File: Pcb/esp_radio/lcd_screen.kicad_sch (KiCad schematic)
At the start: 7 parts, among them J7 LCD I2C, J8 LCD SPI, Q1 AO3415A

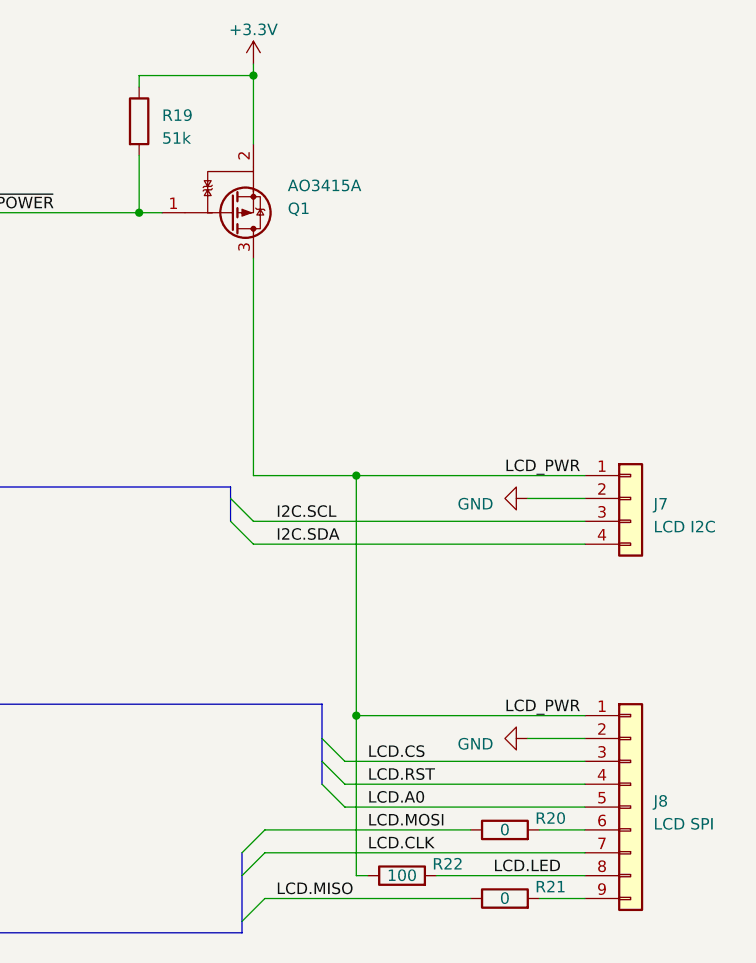
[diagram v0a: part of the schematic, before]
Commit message: Move custom components to kicad_common_library.
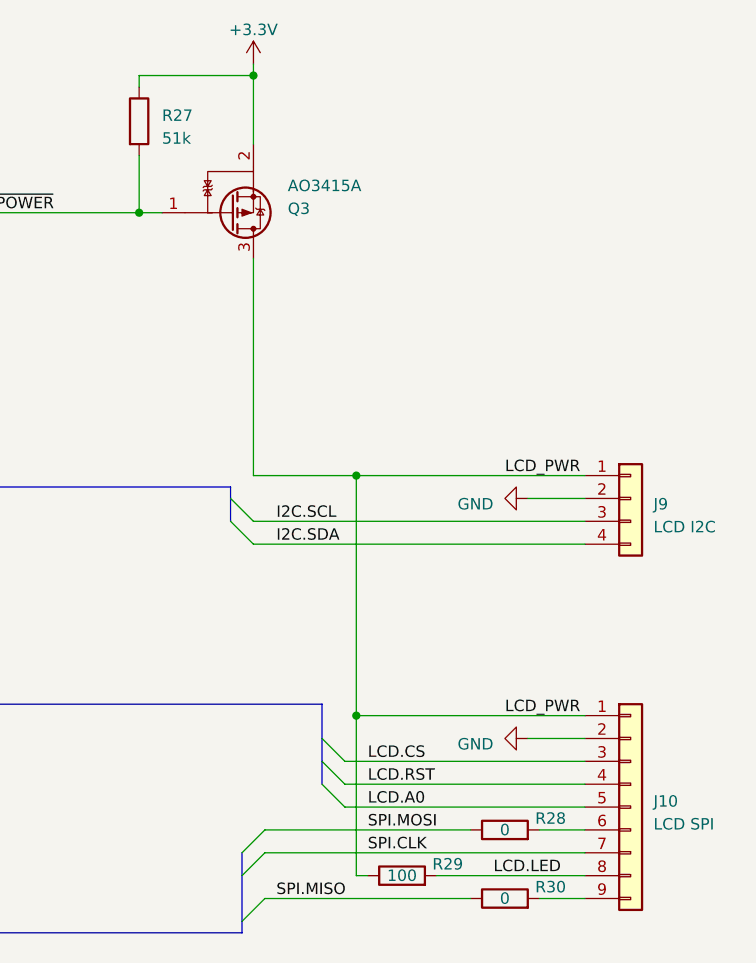
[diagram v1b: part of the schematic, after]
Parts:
- Q3: renamed from Q1; symbol AO3415A:AO3401A -> kicad_common_lib:AO3415A
- renumbered J8 to J10, J7 to J9, R19 to R27, R20 to R28, R22 to R29, R21 to R30
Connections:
- net LCD.CLK renamed SPI.CLK
- net LCD.MISO renamed SPI.MISO
- net LCD.MOSI renamed SPI.MOSI
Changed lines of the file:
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@@
     (effects (font (size 1.27 1.27)) (justify left bottom))
   )
-  (label "LCD.MOSI" (at 185.42 127 0) (fields_autoplaced)
+  (label "SPI.MOSI" (at 185.42 127 0) (fields_autoplaced)
     (effects (font (size 1.27 1.27)) (justify left bottom))
   )
@@
     (effects (font (size 1.27 1.27)) (justify left bottom))
   )
-  (label "LCD.MISO" (at 175.26 134.62 0) (fields_autoplaced)
+  (label "SPI.MISO" (at 175.26 134.62 0) (fields_autoplaced)
     (effects (font (size 1.27 1.27)) (justify left bottom))
   )
@@
     (effects (font (size 1.27 1.27)) (justify left bottom))
   )
-  (label "LCD.CLK" (at 185.42 129.54 0) (fields_autoplaced)
+  (label "SPI.CLK" (at 185.42 129.54 0) (fields_autoplaced)
     (effects (font (size 1.27 1.27)) (justify left bottom))
   )
@@
   (symbol (lib_id "Device:R") (at 200.66 134.62 90) (unit 1)
     (in_bom yes) (on_board yes) (dnp no)
-    (property "Reference" "R21" (at 205.74 133.35 90)
+    (property "Reference" "R30" (at 205.74 133.35 90)
       (effects (font (size 1.27 1.27)))
     )
@@
       (project "esp_radio"
         (path "/c9e2e0d2-0655-4f5e-8e13-71b41b1f7cfe/9a87a4f6-9f89-4802-b675-78042b654f8a"
-          (reference "R21") (unit 1)
+          (reference "R30") (unit 1)
         )
       )
@@
   (symbol (lib_id "Connector_Generic:Conn_01x09") (at 214.63 124.46 0) (unit 1)
     (in_bom yes) (on_board yes) (dnp no) (fields_autoplaced)
-    (property "Reference" "J8" (at 217.17 123.825 0)
+    (property "Reference" "J10" (at 217.17 123.825 0)
       (effects (font (size 1.27 1.27)) (justify left))
     )
@@
       (project "esp_radio"
         (path "/c9e2e0d2-0655-4f5e-8e13-71b41b1f7cfe/9a87a4f6-9f89-4802-b675-78042b654f8a"
-          (reference "J8") (unit 1)
+          (reference "J10") (unit 1)
         )
       )
@@
   (symbol (lib_id "power:GND") (at 203.2 90.17 270) (unit 1)
     (in_bom yes) (on_board yes) (dnp no) (fields_autoplaced)
-    (property "Reference" "#PWR049" (at 196.85 90.17 0)
+    (property "Reference" "#PWR060" (at 196.85 90.17 0)
       (effects (font (size 1.27 1.27)) hide)
     )
@@
       (project "esp_radio"
         (path "/c9e2e0d2-0655-4f5e-8e13-71b41b1f7cfe/9a87a4f6-9f89-4802-b675-78042b654f8a"
-          (reference "#PWR049") (unit 1)
-        )
-      )
-    )
-  )
-  (symbol (lib_id "AO3415A:AO3401A") (at 170.18 58.42 0) (mirror x) (unit 1)
-    (in_bom yes) (on_board yes) (dnp no)
-    (property "Reference" "Q1" (at 176.53 57.9755 0)
+          (reference "#PWR060") (unit 1)
+        )
+      )
+    )
+  )
+  (symbol (lib_id "kicad_common_lib:AO3415A") (at 170.18 58.42 0) (mirror x) (unit 1)
+    (in_bom yes) (on_board yes) (dnp no)
+    (property "Reference" "Q3" (at 176.53 57.9755 0)
       (effects (font (size 1.27 1.27)) (justify left))
     )
@@
       (project "esp_radio"
         (path "/c9e2e0d2-0655-4f5e-8e13-71b41b1f7cfe/9a87a4f6-9f89-4802-b675-78042b654f8a"
-          (reference "Q1") (unit 1)
+          (reference "Q3") (unit 1)
         )
       )
@@
   (symbol (lib_id "Connector_Generic:Conn_01x04") (at 214.63 90.17 0) (unit 1)
     (in_bom yes) (on_board yes) (dnp no) (fields_autoplaced)
-    (property "Reference" "J7" (at 217.17 90.805 0)
+    (property "Reference" "J9" (at 217.17 90.805 0)
       (effects (font (size 1.27 1.27)) (justify left))
     )
@@
       (project "esp_radio"
         (path "/c9e2e0d2-0655-4f5e-8e13-71b41b1f7cfe/9a87a4f6-9f89-4802-b675-78042b654f8a"
-          (reference "J7") (unit 1)
+          (reference "J9") (unit 1)
         )
       )
@@
   (symbol (lib_id "Device:R") (at 160.02 48.26 0) (unit 1)
     (in_bom yes) (on_board yes) (dnp no) (fields_autoplaced)
-    (property "Reference" "R19" (at 162.56 47.625 0)
+    (property "Reference" "R27" (at 162.56 47.625 0)
       (effects (font (size 1.27 1.27)) (justify left))
     )
@@
       (project "esp_radio"
         (path "/c9e2e0d2-0655-4f5e-8e13-71b41b1f7cfe/9a87a4f6-9f89-4802-b675-78042b654f8a"
-          (reference "R19") (unit 1)
+          (reference "R27") (unit 1)
         )
       )
@@
   (symbol (lib_id "power:+3.3V") (at 172.72 41.91 0) (unit 1)
     (in_bom yes) (on_board yes) (dnp no) (fields_autoplaced)
-    (property "Reference" "#PWR050" (at 172.72 45.72 0)
+    (property "Reference" "#PWR059" (at 172.72 45.72 0)
       (effects (font (size 1.27 1.27)) hide)
     )
@@
       (project "esp_radio"
         (path "/c9e2e0d2-0655-4f5e-8e13-71b41b1f7cfe/9a87a4f6-9f89-4802-b675-78042b654f8a"
-          (reference "#PWR050") (unit 1)
+          (reference "#PWR059") (unit 1)
         )
       )
@@
   (symbol (lib_id "Device:R") (at 200.66 127 90) (unit 1)
     (in_bom yes) (on_board yes) (dnp no)
-    (property "Reference" "R20" (at 205.74 125.73 90)
+    (property "Reference" "R28" (at 205.74 125.73 90)
       (effects (font (size 1.27 1.27)))
     )
@@
       (project "esp_radio"
         (path "/c9e2e0d2-0655-4f5e-8e13-71b41b1f7cfe/9a87a4f6-9f89-4802-b675-78042b654f8a"
-          (reference "R20") (unit 1)
+          (reference "R28") (unit 1)
         )
       )
@@
   (symbol (lib_id "Device:R") (at 189.23 132.08 90) (unit 1)
     (in_bom yes) (on_board yes) (dnp no)
-    (property "Reference" "R22" (at 194.31 130.81 90)
+    (property "Reference" "R29" (at 194.31 130.81 90)
       (effects (font (size 1.27 1.27)))
     )
@@
       (project "esp_radio"
         (path "/c9e2e0d2-0655-4f5e-8e13-71b41b1f7cfe/9a87a4f6-9f89-4802-b675-78042b654f8a"
-          (reference "R22") (unit 1)
+          (reference "R29") (unit 1)
         )
       )
@@
   (symbol (lib_id "power:GND") (at 203.2 116.84 270) (unit 1)
     (in_bom yes) (on_board yes) (dnp no) (fields_autoplaced)
-    (property "Reference" "#PWR048" (at 196.85 116.84 0)
+    (property "Reference" "#PWR061" (at 196.85 116.84 0)
       (effects (font (size 1.27 1.27)) hide)
     )
@@
       (project "esp_radio"
         (path "/c9e2e0d2-0655-4f5e-8e13-71b41b1f7cfe/9a87a4f6-9f89-4802-b675-78042b654f8a"
-          (reference "#PWR048") (unit 1)
-        )
-      )
+          (reference "#PWR061") (unit 1)
+        )
+      )

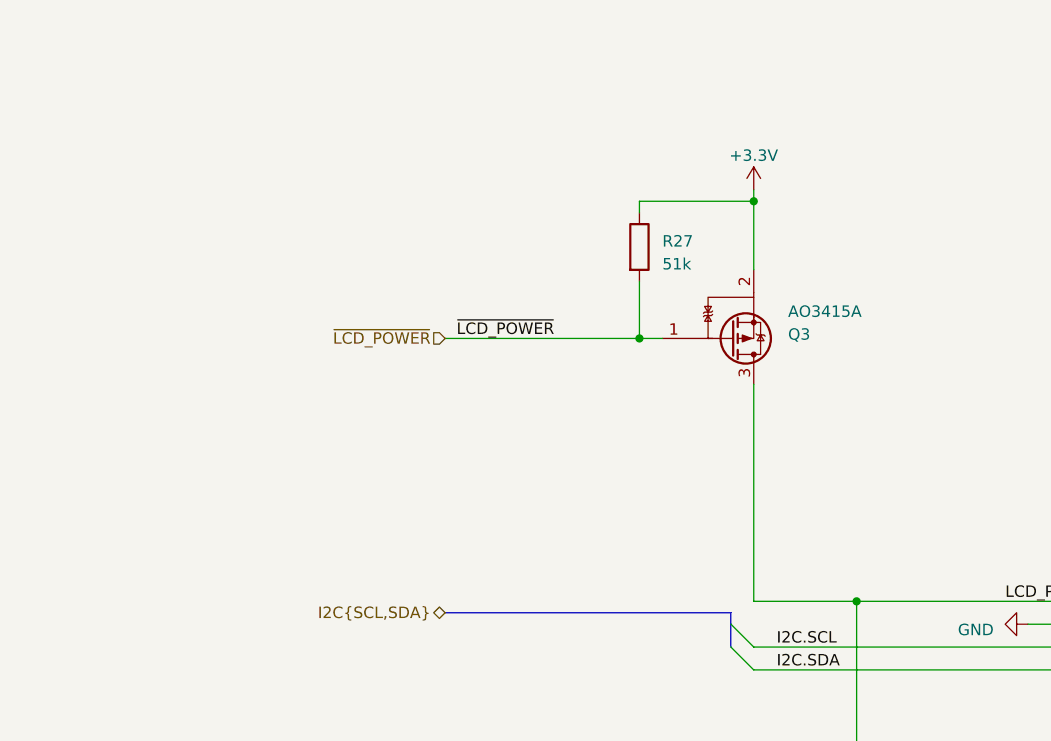
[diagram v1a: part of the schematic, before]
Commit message: Add components layout on PCB
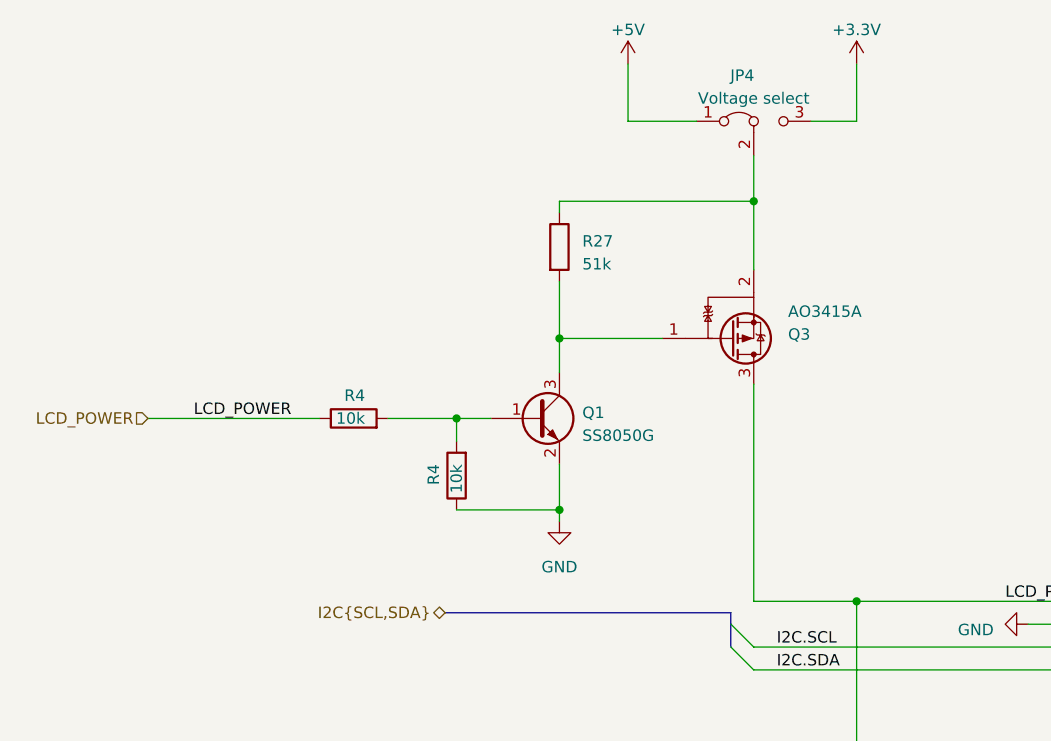
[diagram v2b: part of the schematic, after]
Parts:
- added JP4: Voltage select, Jumper:SolderJumper-3_P1.3mm_Bridged12_Pad1.0x1.5mm, symbol Jumper:Jumper_3_Bridged12
- added Q1: SS8050G, Package_TO_SOT_SMD:SOT-23, symbol kicad_common_lib:SS8050G
- added R4 (x2): 10k, kicad_common_lib:R_0805, symbol Device:R
- J10: footprint (none) -> Connector_JST:JST_XH_S9B-XH-A_1x09_P2.50mm_Horizontal
- J9: footprint (none) -> Connector_JST:JST_XH_S4B-XH-A_1x04_P2.50mm_Horizontal
- R27, R28, R29, R30: footprint (none) -> kicad_common_lib:R_0805
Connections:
- net +3.3V: now also JP4.3 (B); no longer Q3.2 (S), R27.1
- net GND: now also Q1.2 (E), R4.1
- net ~{LCD_POWER}: no longer names the net of Q3.1 (G), R27.2
- net ~{LCD_POWER}: now also Q1.3 (C)
- new net: JP4.2 (C), Q3.2 (S), R27.1
- new net: Q1.1 (B), R4.2, R4.2
- new net +5V: JP4.1 (A)
- new net LCD_POWER: R4.1
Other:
- moved on the sheet: R27

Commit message: Finish board routing
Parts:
- R29: footprint kicad_common_lib:R_0805 -> Resistor_THT:R_Axial_DIN0309_L9.0mm_D3.2mm_P15.24mm_Horizontal
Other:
- note added: "Addr: ST7567S-0b01111xx0"
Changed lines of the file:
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@@
     (stroke (width 0) (type default))
+  )
+  (text "Addr: ST7567S-0b01111xx0" (at 194.31 80.01 0)
+    (effects (font (size 3.27 3.27)) (justify left bottom))
   )
   (label "I2C.SCL" (at 175.26 92.71 0) (fields_autoplaced)
@@
       (effects (font (size 1.27 1.27)))
     )
-    (property "Footprint" "kicad_common_lib:R_0805" (at 189.23 133.858 90)
-      (effects (font (size 1.27 1.27)) hide)
-    )
+    (property "Footprint" "Resistor_THT:R_Axial_DIN0309_L9.0mm_D3.2mm_P15.24mm_Horizontal" (at 189.23 133.858 90)
+      (effects (font (size 1.27 1.27)) hide)
+    )
